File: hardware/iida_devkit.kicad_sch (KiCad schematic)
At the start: 8 parts, among them J1 Tag-Connect 2050

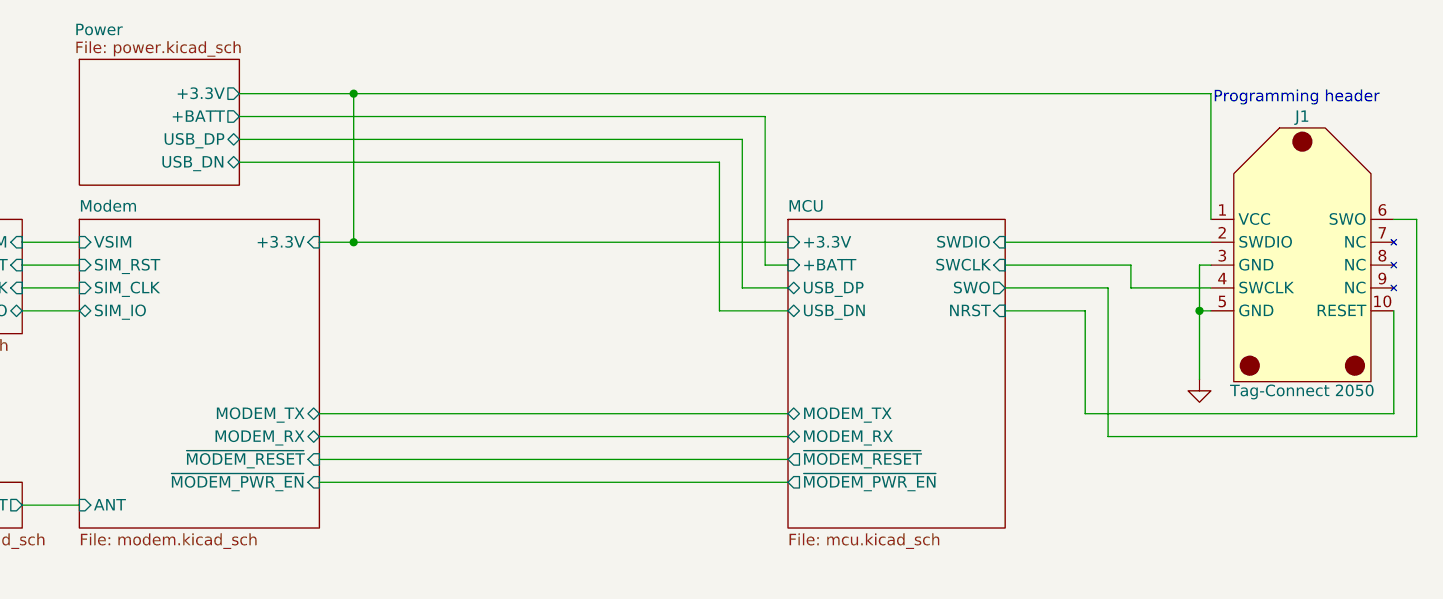
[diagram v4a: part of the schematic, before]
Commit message: HW: Update VBAT, schema and layout
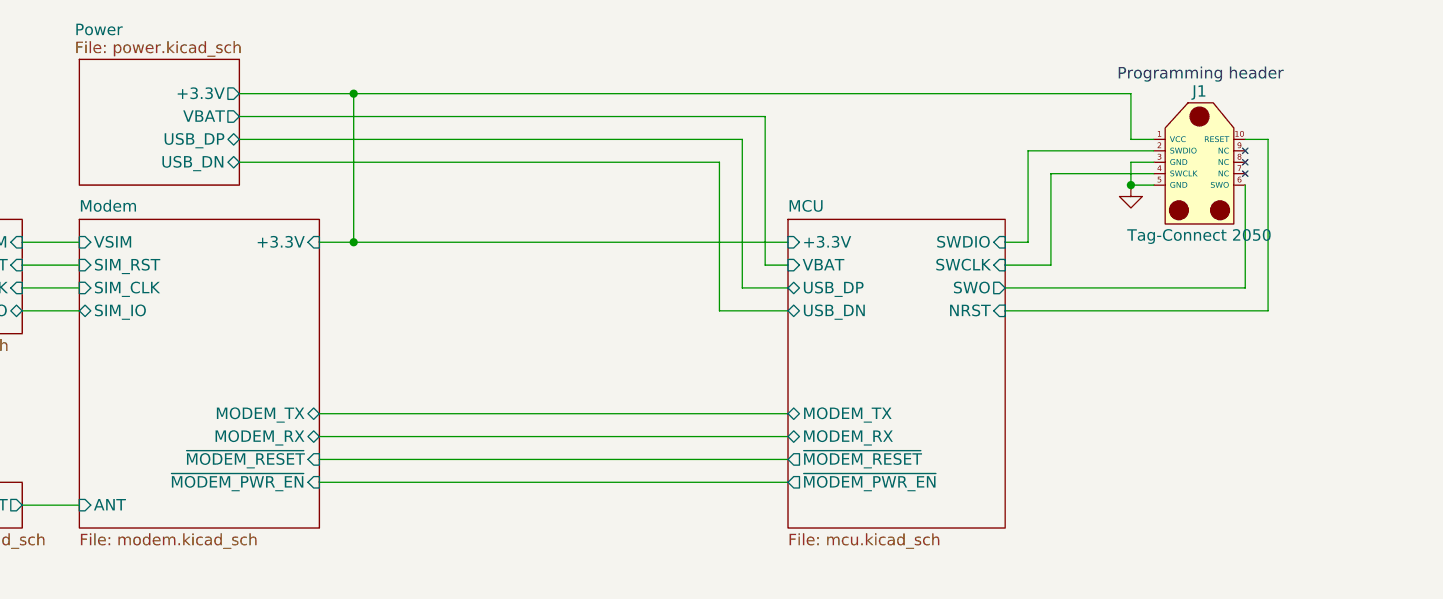
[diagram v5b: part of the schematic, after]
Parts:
- J1: Digi-Key Part Number (none) -> -; Manufacturer (none) -> -; Manufacturer Part Number (none) -> -
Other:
- sheet MCU ports: added VBAT; removed +BATT
- sheet Power ports: added VBAT; removed +BATT
- moved on the sheet: J1
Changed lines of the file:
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@@
 	)
 	(junction
-		(at 223.52 91.44)
+		(at 215.9 77.47)
 		(diameter 0)
 		(color 0 0 0 0)
@@
 	(wire
 		(pts
-			(xy 247.65 105.41) (xy 247.65 81.28)
+			(xy 201.93 83.82) (xy 204.47 83.82)
 		)
 		(stroke
@@
 	(wire
 		(pts
-			(xy 223.52 91.44) (xy 224.79 91.44)
-		)
-		(stroke
-			(width 0)
-			(type default)
-		)
-	)
-	(wire
-		(pts
 			(xy 129.54 67.31) (xy 129.54 83.82)
 		)
@@
 	(wire
 		(pts
-			(xy 223.52 99.06) (xy 223.52 91.44)
-		)
-		(stroke
-			(width 0)
-			(type default)
-		)
-	)
-	(wire
-		(pts
-			(xy 213.36 88.9) (xy 213.36 105.41)
-		)
-		(stroke
-			(width 0)
-			(type default)
-		)
-	)
-	(wire
-		(pts
-			(xy 224.79 88.9) (xy 215.9 88.9)
+			(xy 215.9 77.47) (xy 218.44 77.47)
+		)
+		(stroke
+			(width 0)
+			(type default)
+		)
+	)
+	(wire
+		(pts
+			(xy 231.14 91.44) (xy 231.14 72.39)
+		)
+		(stroke
+			(width 0)
+			(type default)
+		)
+	)
+	(wire
+		(pts
+			(xy 231.14 72.39) (xy 228.6 72.39)
+		)
+		(stroke
+			(width 0)
+			(type default)
+		)
+	)
+	(wire
+		(pts
+			(xy 201.93 88.9) (xy 228.6 88.9)
 		)
 		(stroke
@@
 	(wire
 		(pts
-			(xy 215.9 88.9) (xy 215.9 86.36)
-		)
-		(stroke
-			(width 0)
-			(type default)
-		)
-	)
-	(wire
-		(pts
-			(xy 224.79 86.36) (xy 223.52 86.36)
-		)
-		(stroke
-			(width 0)
-			(type default)
-		)
-	)
-	(wire
-		(pts
-			(xy 210.82 91.44) (xy 201.93 91.44)
+			(xy 218.44 74.93) (xy 215.9 74.93)
 		)
 		(stroke
@@
 	(wire
 		(pts
-			(xy 210.82 102.87) (xy 210.82 91.44)
-		)
-		(stroke
-			(width 0)
-			(type default)
-		)
-	)
-	(wire
-		(pts
-			(xy 245.11 102.87) (xy 210.82 102.87)
-		)
-		(stroke
-			(width 0)
-			(type default)
-		)
-	)
-	(wire
-		(pts
-			(xy 201.93 88.9) (xy 213.36 88.9)
+			(xy 201.93 91.44) (xy 231.14 91.44)
+		)
+		(stroke
+			(width 0)
+			(type default)
+		)
+	)
+	(wire
+		(pts
+			(xy 204.47 73.66) (xy 218.44 73.66)
 		)
 		(stroke
@@
 	(wire
 		(pts
-			(xy 245.11 91.44) (xy 245.11 102.87)
+			(xy 215.9 72.39) (xy 218.44 72.39)
 		)
 		(stroke
@@
 	(wire
 		(pts
-			(xy 224.79 67.31) (xy 129.54 67.31)
-		)
-		(stroke
-			(width 0)
-			(type default)
-		)
-	)
-	(wire
-		(pts
 			(xy 125.73 83.82) (xy 129.54 83.82)
 		)
@@
 	(wire
 		(pts
+			(xy 207.01 76.2) (xy 218.44 76.2)
+		)
+		(stroke
+			(width 0)
+			(type default)
+		)
+	)
+	(wire
+		(pts
 			(xy 92.71 88.9) (xy 99.06 88.9)
 		)
@@
 	(wire
 		(pts
+			(xy 215.9 74.93) (xy 215.9 77.47)
+		)
+		(stroke
+			(width 0)
+			(type default)
+		)
+	)
+	(wire
+		(pts
 			(xy 125.73 110.49) (xy 177.8 110.49)
 		)
@@
 	(wire
 		(pts
+			(xy 204.47 83.82) (xy 204.47 73.66)
+		)
+		(stroke
+			(width 0)
+			(type default)
+		)
+	)
+	(wire
+		(pts
+			(xy 215.9 67.31) (xy 215.9 72.39)
+		)
+		(stroke
+			(width 0)
+			(type default)
+		)
+	)
+	(wire
+		(pts
 			(xy 92.71 113.03) (xy 99.06 113.03)
 		)
@@
 	(wire
 		(pts
-			(xy 224.79 67.31) (xy 224.79 81.28)
-		)
-		(stroke
-			(width 0)
-			(type default)
-		)
-	)
-	(wire
-		(pts
-			(xy 223.52 86.36) (xy 223.52 91.44)
-		)
-		(stroke
-			(width 0)
-			(type default)
-		)
-	)
-	(wire
-		(pts
-			(xy 201.93 83.82) (xy 224.79 83.82)
-		)
-		(stroke
-			(width 0)
-			(type default)
-		)
-	)
-	(wire
-		(pts
-			(xy 247.65 81.28) (xy 245.11 81.28)
-		)
-		(stroke
-			(width 0)
-			(type default)
-		)
-	)
-	(wire
-		(pts
 			(xy 177.8 88.9) (xy 172.72 88.9)
 		)
@@
 	(wire
 		(pts
-			(xy 215.9 86.36) (xy 201.93 86.36)
-		)
-		(stroke
-			(width 0)
-			(type default)
-		)
-	)
-	(wire
-		(pts
 			(xy 116.84 74.93) (xy 170.18 74.93)
 		)
@@
 	(wire
 		(pts
+			(xy 201.93 86.36) (xy 207.01 86.36)
+		)
+		(stroke
+			(width 0)
+			(type default)
+		)
+	)
+	(wire
+		(pts
+			(xy 129.54 67.31) (xy 215.9 67.31)
+		)
+		(stroke
+			(width 0)
+			(type default)
+		)
+	)
+	(wire
+		(pts
 			(xy 129.54 83.82) (xy 177.8 83.82)
 		)
@@
 	(wire
 		(pts
-			(xy 213.36 105.41) (xy 247.65 105.41)
+			(xy 207.01 86.36) (xy 207.01 76.2)
 		)
 		(stroke
@@
 		(pts
 			(xy 92.71 91.44) (xy 99.06 91.44)
+		)
+		(stroke
+			(width 0)
+			(type default)
+		)
+	)
+	(wire
+		(pts
+			(xy 228.6 88.9) (xy 228.6 77.47)
 		)
 		(stroke
@@
 	(text "Programming header"
 		(exclude_from_sim no)
-		(at 225.044 67.818 0)
+		(at 214.376 65.278 0)
 		(effects
 			(font
@@
 	(symbol
 		(lib_id "power:GND")
-		(at 223.52 99.06 0)
+		(at 215.9 77.47 0)
 		(unit 1)
 		(exclude_from_sim no)
@@
 		(fields_autoplaced yes)
 		(property "Reference" "#PWR02"
-			(at 223.52 105.41 0)
+			(at 215.9 83.82 0)
 			(effects
 				(font
@@
 		)
 		(property "Value" "GND"
-			(at 223.52 104.14 0)
+			(at 215.9 82.55 0)
 			(effects
 				(font
@@
 		)
 		(property "Footprint" ""
-			(at 223.52 99.06 0)
+			(at 215.9 77.47 0)
 			(effects
 				(font
@@
 		)
 		(property "Datasheet" ""
-			(at 223.52 99.06 0)
+			(at 215.9 77.47 0)
 			(effects
 				(font
@@
 		)
 		(property "Description" "Power symbol creates a global label with name \"GND\" , ground"
-			(at 223.52 99.06 0)
+			(at 215.9 77.47 0)
 			(effects
 				(font
@@
 	(symbol
 		(lib_id "Tag-Connect:TC2050")
-		(at 234.95 86.36 0)
+		(at 223.52 74.93 0)
 		(mirror y)
 		(unit 1)
@@
 		(dnp no)
 		(property "Reference" "J1"
-			(at 234.95 69.85 0)
+			(at 223.52 67.056 0)
 			(effects
 				(font
@@
 		)
 		(property "Value" "Tag-Connect 2050"
-			(at 234.95 100.33 0)
+			(at 223.52 83.058 0)
 			(effects
 				(font
@@
 		)
 		(property "Footprint" "Connector:Tag-Connect_TC2050-IDC-FP_2x05_P1.27mm_Vertical"
-			(at 234.95 103.378 0)
+			(at 223.52 91.948 0)
 			(effects
 				(font
@@
 		)
 		(property "Datasheet" "https://www.tag-connect.com/wp-content/uploads/bsk-pdf-manager/2021/02/TC2050-ARM2010-2021.pdf"
-			(at 234.95 103.378 0)
+			(at 223.52 91.948 0)
 			(effects
 				(font
@@
 		)
 		(property "Description" "ARM 20-pin to ARM 10-pin JTAG or ARM SWD adapter"
-			(at 234.95 103.378 0)
+			(at 223.52 91.948 0)
+			(effects
+				(font
+					(size 1.27 1.27)
+				)
+				(hide yes)
+			)
+		)
+		(property "Digi-Key Part Number" "-"
+			(at 223.52 74.93 0)
+			(effects
+				(font
+					(size 1.27 1.27)
+				)
+				(hide yes)
+			)
+		)
+		(property "Manufacturer" "-"
+			(at 223.52 74.93 0)
+			(effects
+				(font
+					(size 1.27 1.27)
+				)
+				(hide yes)
+			)
+		)
+		(property "Manufacturer Part Number" "-"
+			(at 223.52 74.93 0)
 			(effects
 				(font
@@
 			)
 		)
-		(pin "+BATT" input
+		(pin "VBAT" input
 			(at 177.8 86.36 180)
 			(effects
@@
 			)
 		)
-		(pin "+BATT" output
+		(pin "VBAT" output
 			(at 116.84 69.85 0)
 			(effects

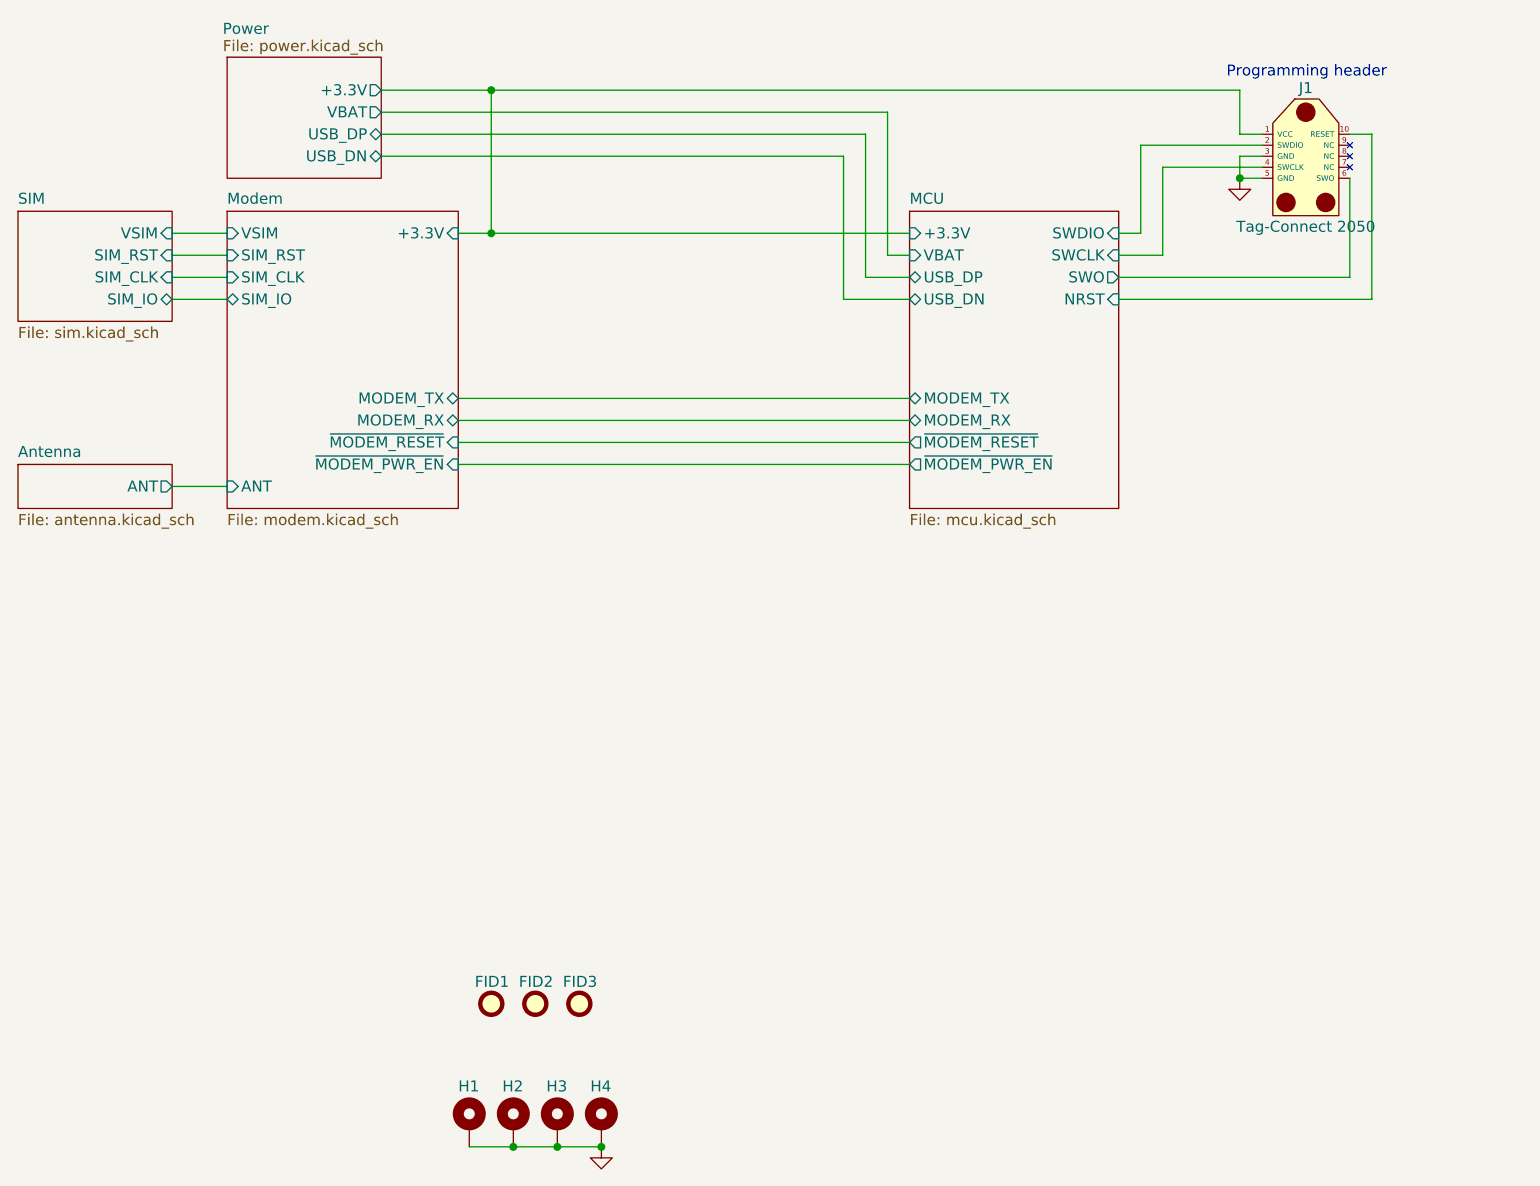
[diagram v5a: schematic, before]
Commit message: HW: Start adding Li-Po support
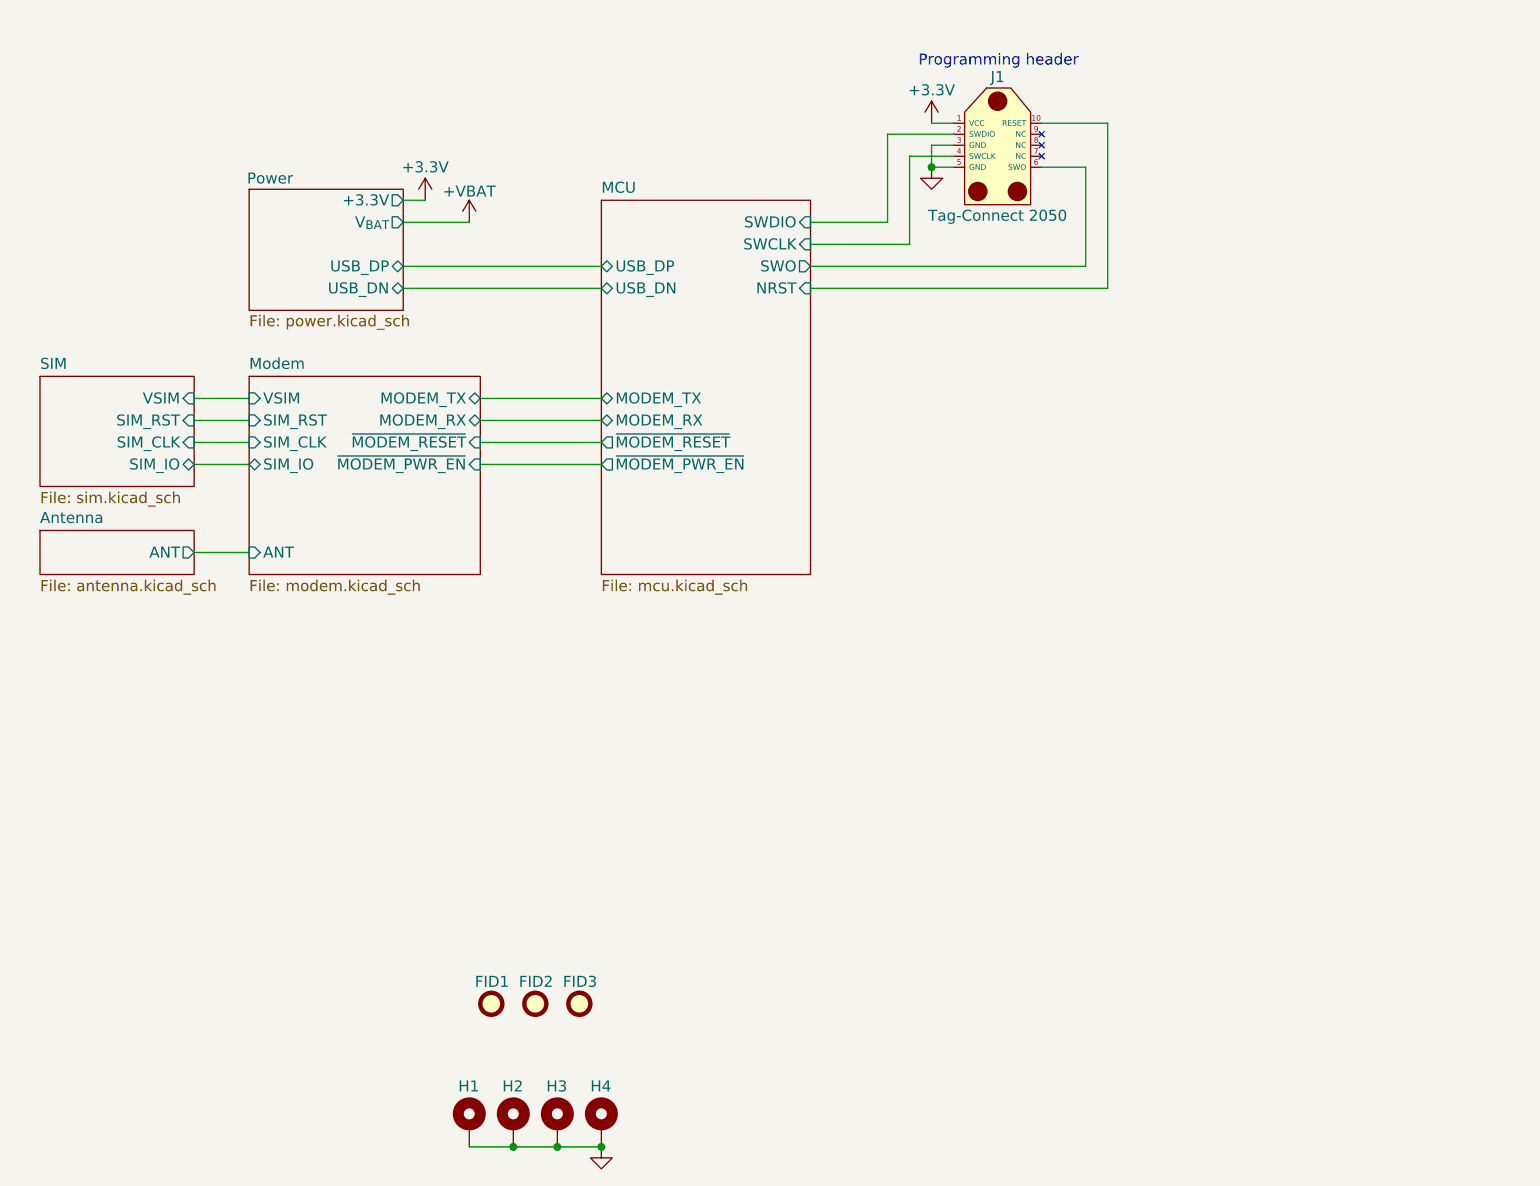
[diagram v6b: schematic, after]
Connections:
- net MCU/+3.3V renamed +3.3V
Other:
- sheet MCU ports: added none; removed +3.3V, VBAT
- sheet Modem ports: added none; removed +3.3V
- sheet Power ports: added V_{BAT}; removed VBAT
- moved on the sheet: J1

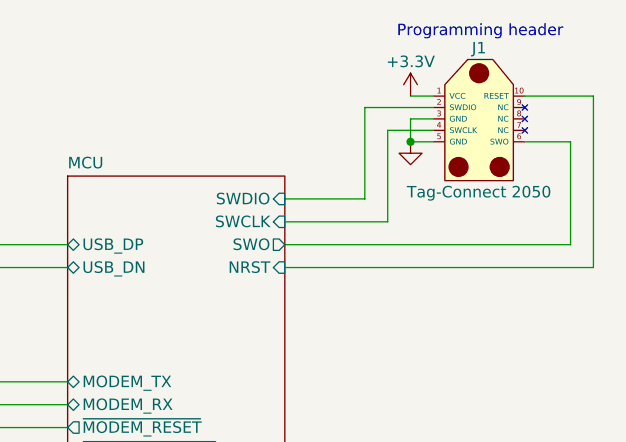
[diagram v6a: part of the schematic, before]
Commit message: HW: Replace TC2050 wiht 10-pin connector
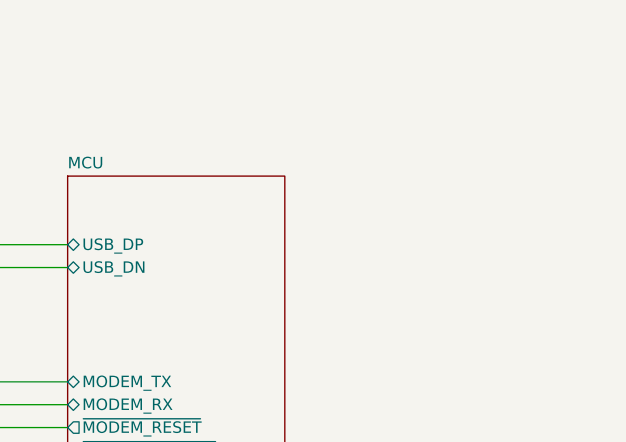
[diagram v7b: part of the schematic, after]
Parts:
- removed J1: Tag-Connect 2050, Connector:Tag-Connect_TC2050-IDC-FP_2x05_P1.27mm_Vertical, symbol Tag-Connect:TC2050
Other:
- sheet MCU ports: added none; removed NRST, SWCLK, SWDIO, SWO
- note removed: "Programming header"

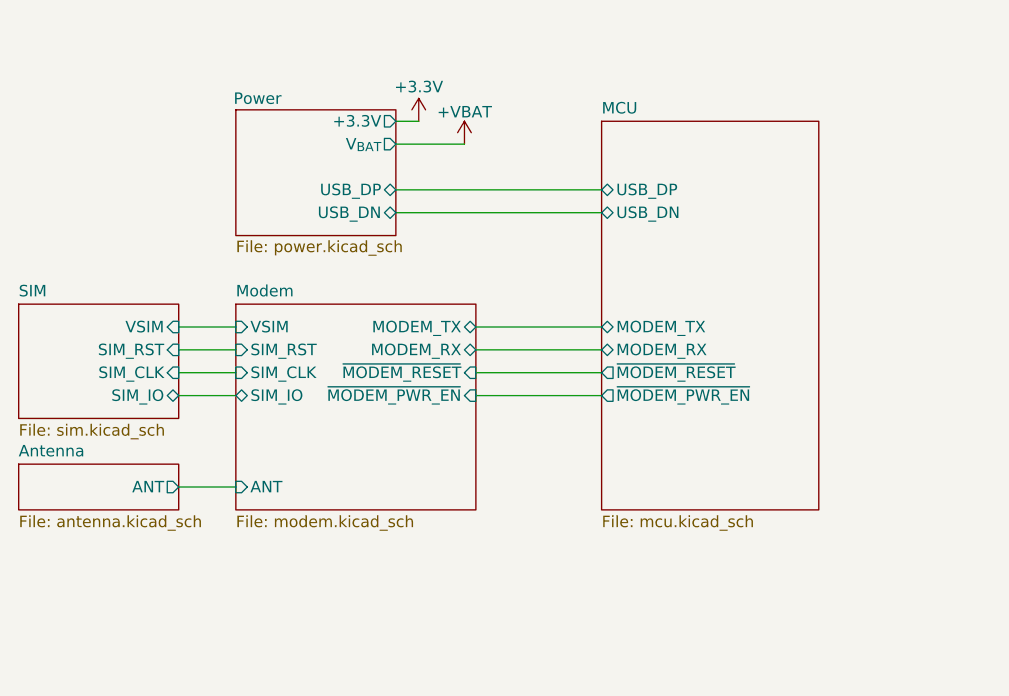
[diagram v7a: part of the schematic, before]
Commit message: HW: Cleanup schematic
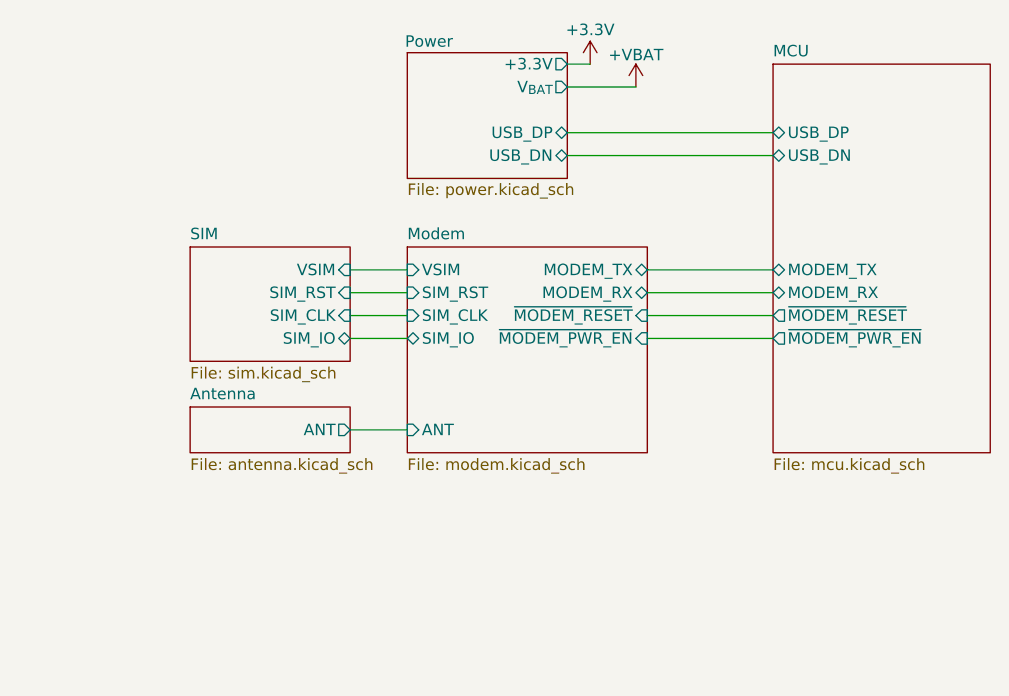
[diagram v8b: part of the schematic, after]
